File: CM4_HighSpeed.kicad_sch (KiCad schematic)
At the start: 10 parts, among them J13 1-2199119-5, J15 USB_OTG, J16 Conn_01x02, J3 USB-A-S-VT, J5 690-019-298-412, U11 TPD4EUSB30, U13 RT9742SNGV

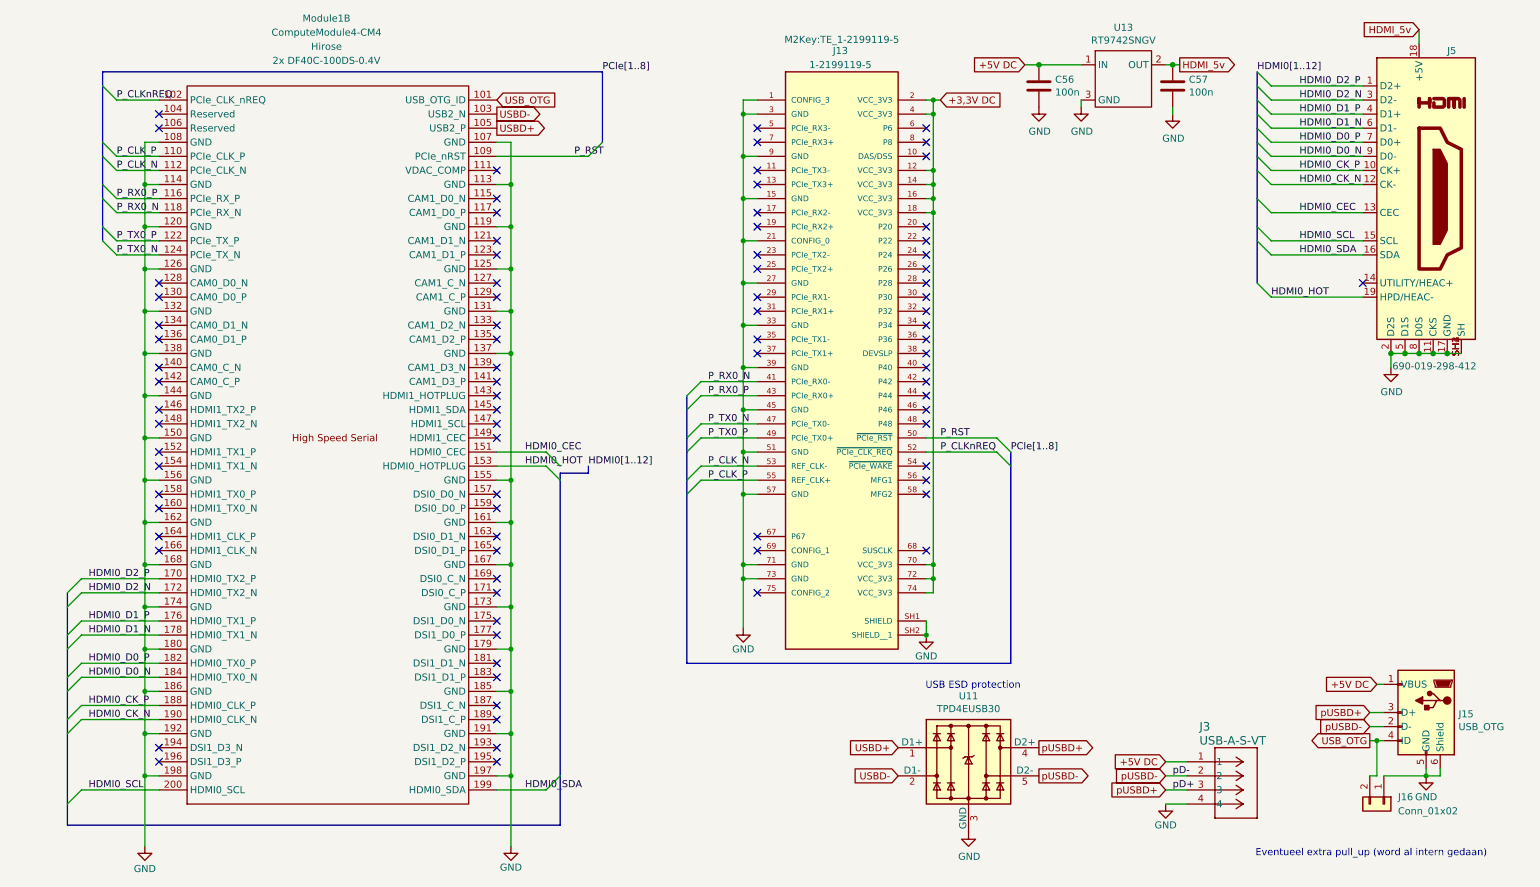
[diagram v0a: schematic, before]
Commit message: Redid the routing and fixed ERC warnings
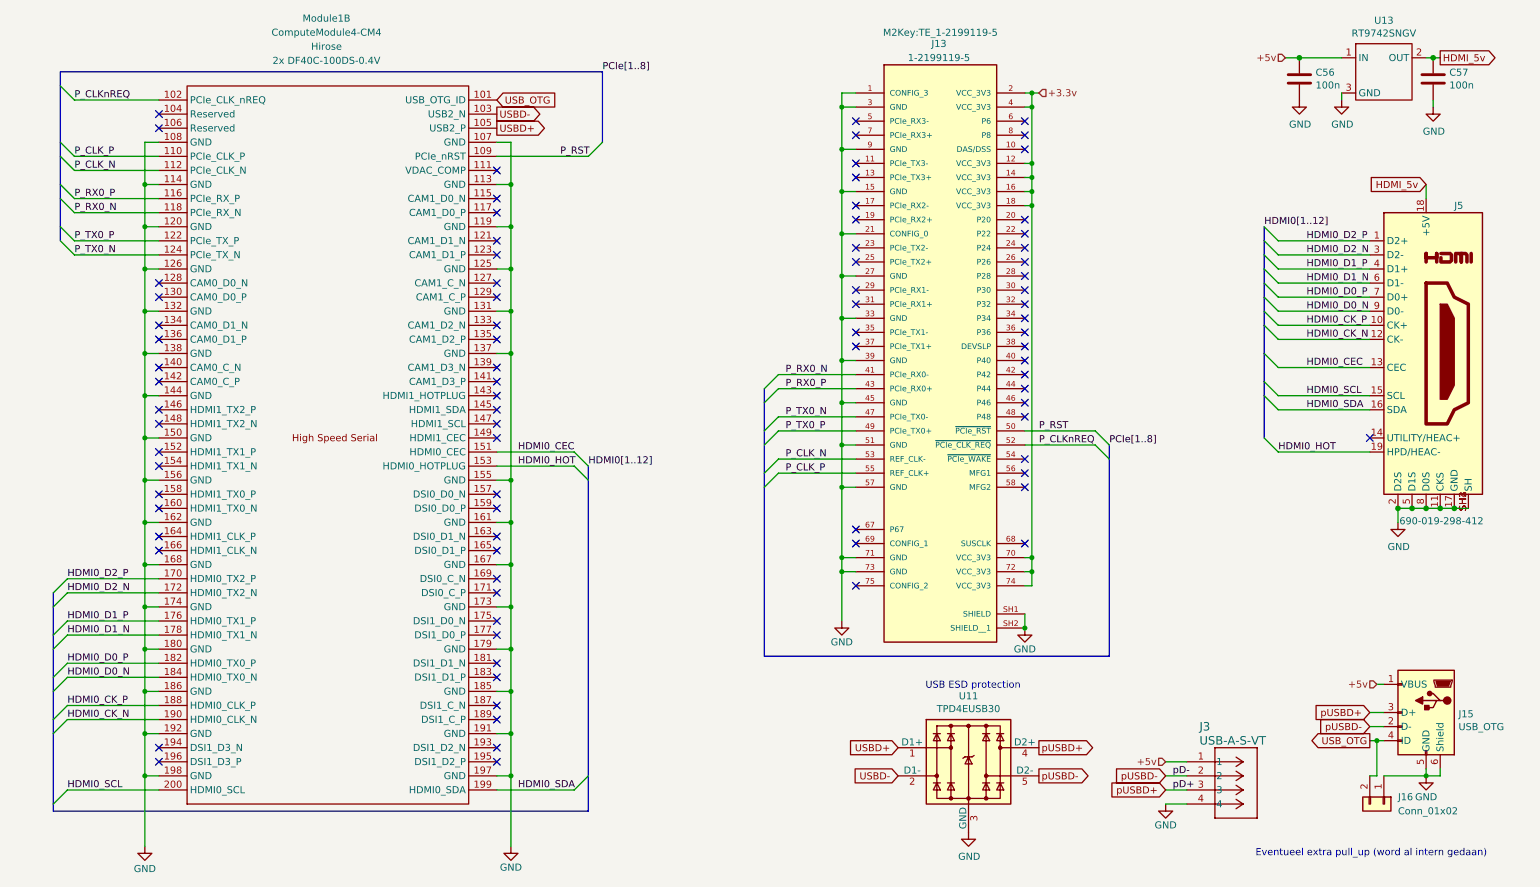
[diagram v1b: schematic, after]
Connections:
- net +3,3V DC renamed +3.3v
- net +5V DC renamed +5v
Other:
- moved on the sheet: C56, C57, J13, J5, U13

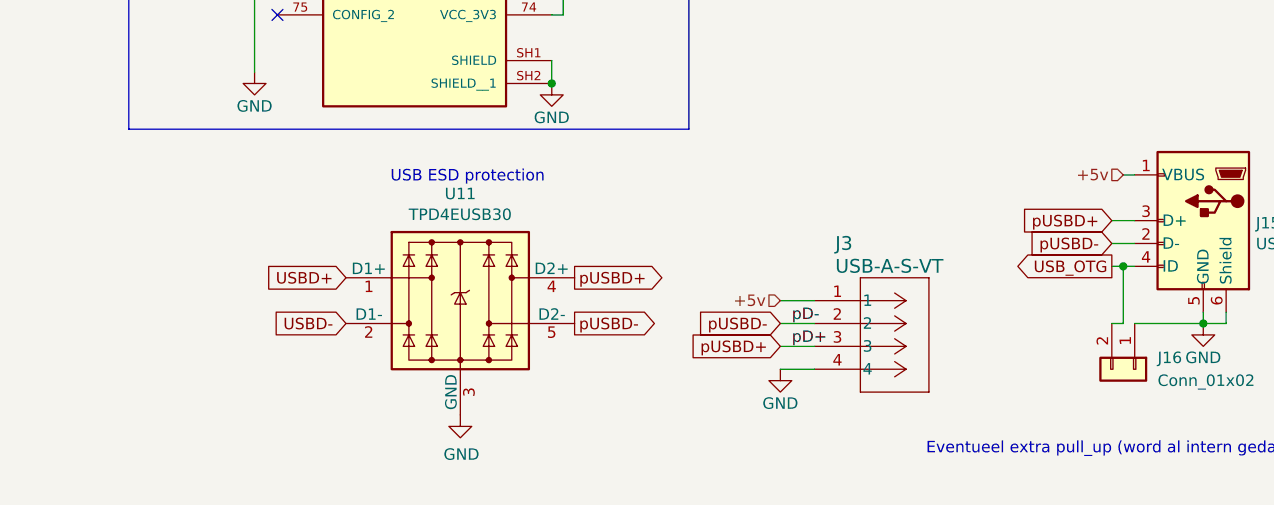
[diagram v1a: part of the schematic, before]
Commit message: Redid traces with correct requirements, needs double checking.
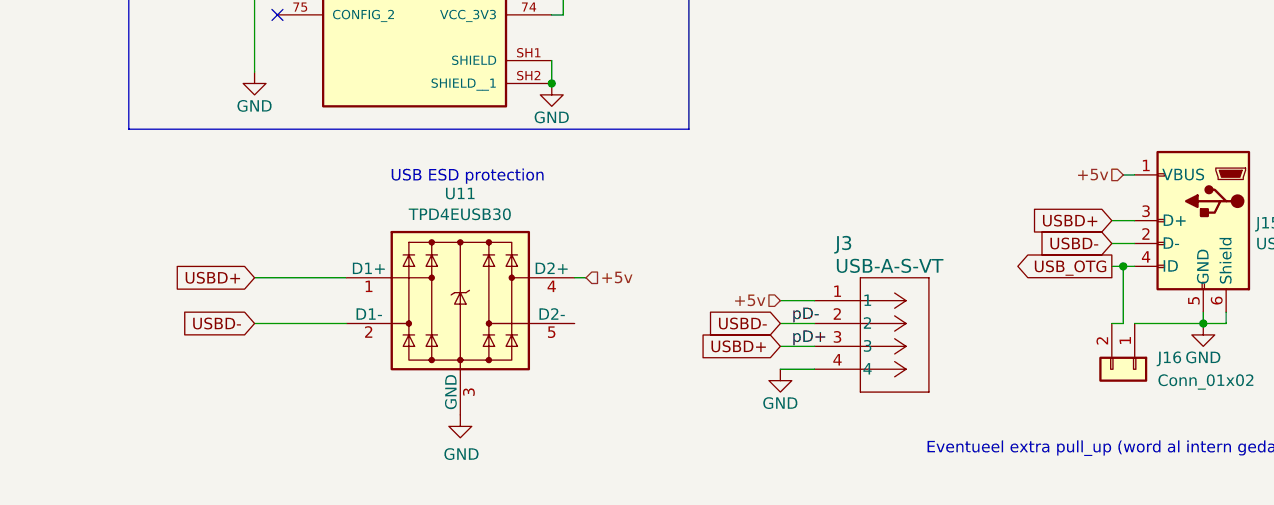
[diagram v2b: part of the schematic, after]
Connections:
- net +5v: now also U11.4 (D2+), U11.7
- net USBD+: now also J15.3 (D+), J3.3
- net USBD-: now also J15.2 (D-), J3.2
- removed net pUSBD+: J15.3 (D+), J3.3, U11.4 (D2+), U11.7
- net pUSBD-: no longer names the net of U11.5 (D2-), U11.6
- net pUSBD-: no longer J15.2 (D-), J3.2
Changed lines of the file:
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@@
+	(wire
+		(pts
+			(xy 165.1 149.86) (xy 175.26 149.86)
+		)
+		(stroke
+			(width 0)
+			(type default)
+		)
+	)
 	(wire
 		(pts
@@
 		)
 	)
+	(wire
+		(pts
+			(xy 200.66 144.78) (xy 201.93 144.78)
+		)
+		(stroke
+			(width 0)
+			(type default)
+		)
+	)
 	(bus
 		(pts
@@
 		(pts
 			(xy 241.3 81.28) (xy 241.3 88.9)
+		)
+		(stroke
+			(width 0)
+			(type default)
+		)
+	)
+	(wire
+		(pts
+			(xy 165.1 144.78) (xy 175.26 144.78)
 		)
 		(stroke
@@
 		)
 	)
-	(global_label "pUSBD-"
+	(global_label "USBD-"
 		(shape input)
 		(at 223.52 149.86 180)
@@
 		)
 		(property "Intersheetrefs" "${INTERSHEET_REFS}"
-			(at 212.7334 149.86 0)
+			(at 213.8824 149.86 0)
 			(effects
 				(font
@@
 	(global_label "USBD-"
 		(shape input)
-		(at 175.26 149.86 180)
+		(at 165.1 149.86 180)
 		(fields_autoplaced yes)
 		(effects
@@
 		)
 		(property "Intersheetrefs" "${INTERSHEET_REFS}"
-			(at 165.6224 149.86 0)
+			(at 155.4624 149.86 0)
 			(effects
 				(font
@@
 	(global_label "USBD+"
 		(shape input)
-		(at 175.26 144.78 180)
+		(at 165.1 144.78 180)
 		(fields_autoplaced yes)
 		(effects
@@
 		)
 		(property "Intersheetrefs" "${INTERSHEET_REFS}"
-			(at 165.6224 144.78 0)
+			(at 155.4624 144.78 0)
 			(effects
 				(font
@@
 				)
 				(justify right)
-				(hide yes)
-			)
-		)
-	)
-	(global_label "pUSBD-"
-		(shape output)
-		(at 200.66 149.86 0)
-		(fields_autoplaced yes)
-		(effects
-			(font
-				(size 1.27 1.27)
-			)
-			(justify left)
-		)
-		(property "Intersheetrefs" "${INTERSHEET_REFS}"
-			(at 211.4466 149.86 0)
-			(effects
-				(font
-					(size 1.27 1.27)
-				)
-				(justify left)
 				(hide yes)
 			)
@@
 		)
 	)
-	(global_label "pUSBD+"
+	(global_label "USBD+"
 		(shape input)
 		(at 260.35 138.43 180)
@@
 		)
 		(property "Intersheetrefs" "${INTERSHEET_REFS}"
-			(at 249.5634 138.43 0)
+			(at 250.7124 138.43 0)
 			(effects
 				(font
@@
 		)
 	)
-	(global_label "pUSBD-"
+	(global_label "USBD-"
 		(shape input)
 		(at 260.35 140.97 180)
@@
 		)
 		(property "Intersheetrefs" "${INTERSHEET_REFS}"
-			(at 249.5634 140.97 0)
+			(at 250.7124 140.97 0)
 			(effects
 				(font
@@
 		)
 	)
-	(global_label "pUSBD+"
+	(global_label "USBD+"
 		(shape input)
 		(at 223.52 152.4 180)
@@
 		)
 		(property "Intersheetrefs" "${INTERSHEET_REFS}"
-			(at 212.7334 152.4 0)
+			(at 213.8824 152.4 0)
 			(effects
 				(font
@@
 		)
 	)
-	(global_label "pUSBD+"
-		(shape output)
-		(at 200.66 144.78 0)
-		(fields_autoplaced yes)
+	(hierarchical_label "+5v"
+		(shape input)
+		(at 201.93 144.78 0)
 		(effects
 			(font
@@
 			(justify left)
 		)
-		(property "Intersheetrefs" "${INTERSHEET_REFS}"
-			(at 211.4466 144.78 0)
-			(effects
-				(font
-					(size 1.27 1.27)
-				)
-				(justify left)
-				(hide yes)
-			)
-		)
-	)
+	)

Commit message: Hehe, smol board now
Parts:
- removed J15: USB_OTG, Connector_USB:USB_Micro-B_Amphenol_10103594-0001LF_Horizontal, symbol Connector:USB_OTG
- removed J16: Conn_01x02, Connector_PinHeader_2.54mm:PinHeader_1x02_P2.54mm_Vertical, symbol Connector_Generic:Conn_01x02
- added J2: 2036150003 (USB-C_Connector), USB-C:CONN_2036150003_MOL(USB-c_connector), symbol 2026-03-08_10-34-21:2036150003
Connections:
- net +5v: now also J2.A4 (VBUS), J2.A9 (VBUS), J2.B4 (VBUS), J2.B9 (VBUS)
- net GND: now also J2.A1 (GND), J2.A12 (GND), J2.B1 (GND), J2.B12 (GND), J2.GND1 (GND), J2.GND2 (GND)
- net USBD+: now also J2.A6 (D+), J2.B6 (D+)
- net USBD-: now also J2.A7 (D-), J2.B7 (D-)
- no-connect marks 85 -> 89
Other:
- moved on the sheet: C56, C57, J13, J3, J5, Module1B, U11, U13

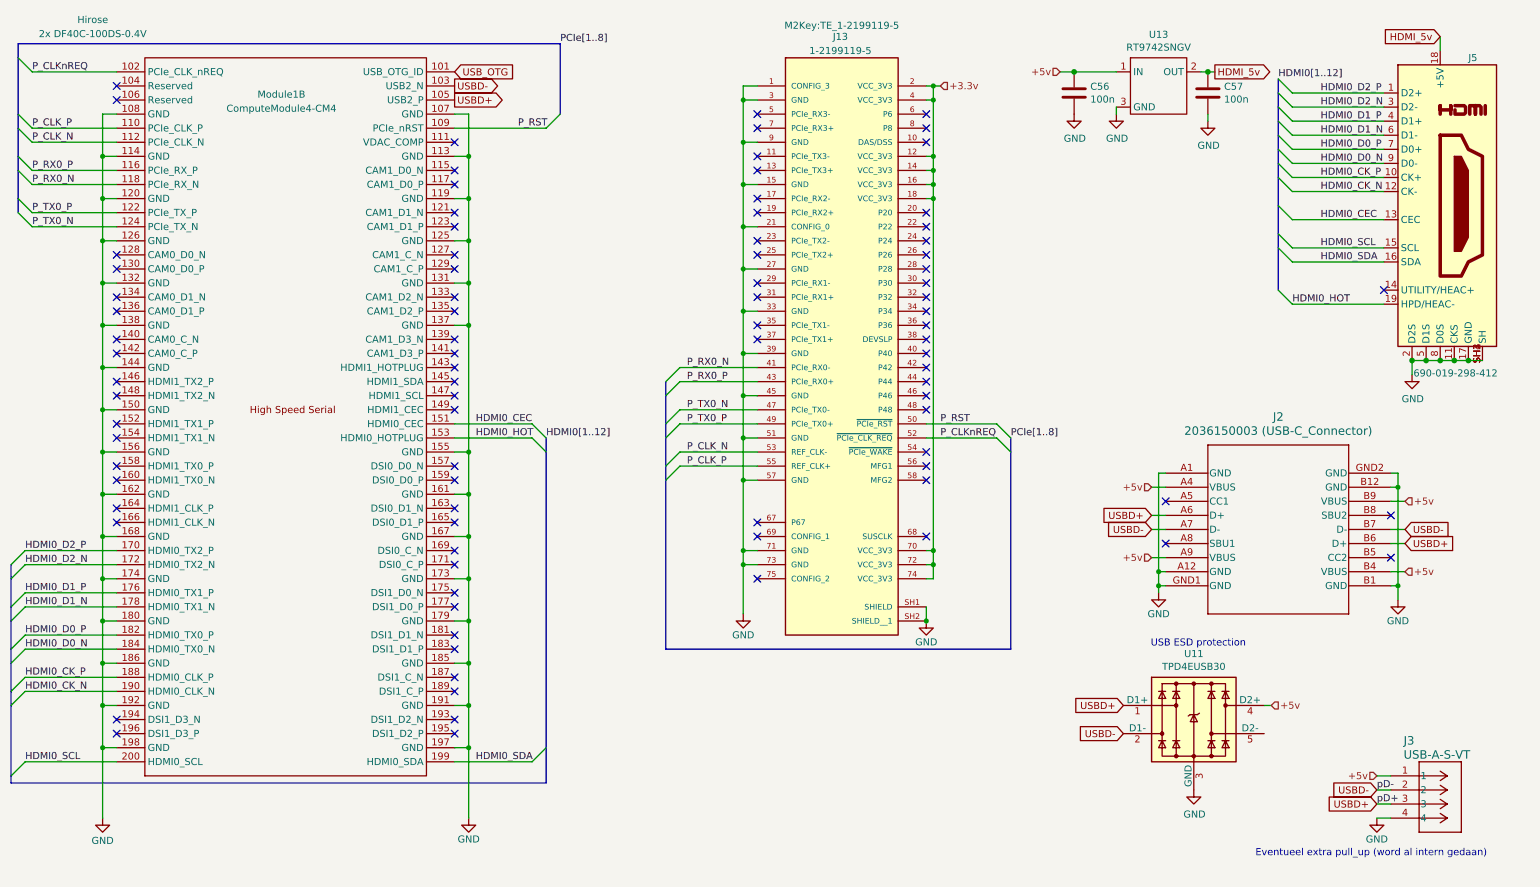
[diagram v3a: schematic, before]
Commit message: Changed quite a bit, PCB smoll now
Redid all traces, replaced HUSB238 with ch224k, made PCB even smaller.
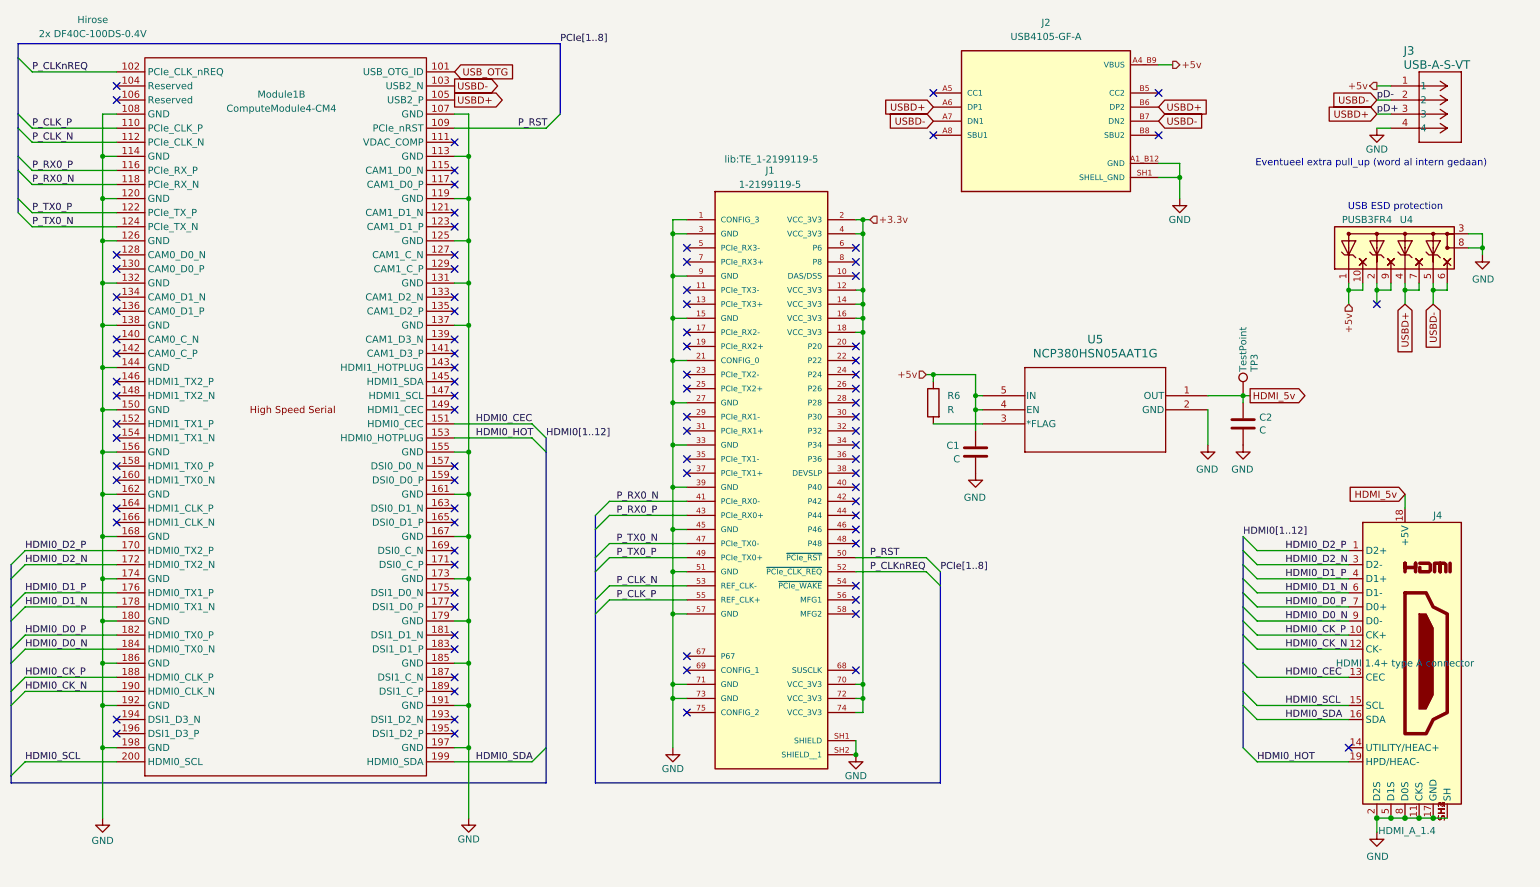
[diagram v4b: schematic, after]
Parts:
- removed C56: 100n, Capacitor_SMD:C_0402_1005Metric_Pad0.74x0.62mm_HandSolder, symbol Device:C
- removed J2: 2036150003 (USB-C_Connector), USB-C:CONN_2036150003_MOL(USB-c_connector), symbol 2026-03-08_10-34-21:2036150003
- removed U11: TPD4EUSB30, Package_SON:USON-10_2.5x1.0mm_P0.5mm, symbol CM4IO:TPD4EUSB30
- removed U13: RT9742SNGV, Package_TO_SOT_SMD:SOT-23, symbol CM4IO:RT9742SNGV
- added C2: C, Capacitor_SMD:C_0402_1005Metric_Pad0.74x0.62mm_HandSolder, symbol Device:C
- added J2: USB4105-GF-A, USB4105-GF-A:GCT_USB4105-GF-A, symbol USB4105-GF-A:USB4105-GF-A
- added R6: R, Resistor_SMD:R_0402_1005Metric_Pad0.72x0.64mm_HandSolder, symbol Device:R
- added TP3: TestPoint, TestPoint:TestPoint_Pad_2.0x2.0mm, symbol Connector:TestPoint
- added U4: PUSB3FR4, lib:SOT1176-1, symbol PUSB3FR4:PUSB3FR4
- added U5: NCP380HSN05AAT1G, TSOP-5_ONS, symbol NCP380HSN05AAT1G:NCP380HSN05AAT1G
- C1: renamed from C57; value 100n -> C
- J1: renamed from J13; footprint M2Key:TE_1-2199119-5 -> lib:TE_1-2199119-5
- J3: footprint USB-A-S-VT:CONN_USB-A-S-VT_ADM -> CONN_USB-A-S-VT_ADM
- J4: renamed from J5; value 690-019-298-412 -> HDMI_A_1.4
- Module1: footprint ComputeModule4:Raspberry-Pi-4-Compute-Module -> CM4IO:Raspberry-Pi-4-Compute-Module
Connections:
- net GND: now also C2.2, J2.A1_B12 (GND), J2.B1_A12 (GND), J2.SH1 (SHELL_GND), J2.SH2 (SHELL_GND), J2.SH3 (SHELL_GND), J2.SH4 (SHELL_GND), U4.3 (GND), U4.8 (GND), U5.2 (GND)
- net HDMI_5v: now also C2.1, TP3.1, U5.1 (OUT); no longer C1.1
- net USBD+: now also J2.A6 (DP1), J2.B6 (DP2), U4.4 (In_1+), U4.7 (Out_1+)
- net USBD-: now also J2.A7 (DN1), J2.B7 (DN2), U4.5 (In_1-), U4.6 (Out_1+)
- net +5v renamed VBUS
- net VBUS: now also C1.1, J2.A4_B9 (VBUS), J2.B4_A9 (VBUS), R6.1, U4.1 (In_1+), U4.10 (Out_1+), U5.4 (EN), U5.5 (IN)
- new net: R6.2, U5.3 (*FLAG)
- new net: U4.2 (In_1-), U4.9 (Out_1+)
- no-connect marks 89 -> 90
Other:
- moved on the sheet: C1, J1, J3, J4

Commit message: Added datasheets for to-be-ordered components, double checked BOM
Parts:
- C1: value C -> 10u
- R6: value R -> 100k
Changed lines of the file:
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@@
 			)
 		)
-		(property "Value" "C"
+		(property "Value" "10u"
 			(at 186.436 92.71 0)
 			(effects
@@
 			)
 		)
-		(property "Value" "R"
+		(property "Value" "100k"
 			(at 184.15 83.8199 0)
 			(effects
